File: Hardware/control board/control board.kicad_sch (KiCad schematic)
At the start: 11 parts, among them J1 Screw_Terminal_01x02, SW1 SW_Push

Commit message: updated Board design to v2
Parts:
- added D7: LED, LED_THT:LED_D3.0mm_Clear, symbol Device:LED
- added E10, E9: Conn_01x03_Pin, Connector_PinHeader_2.54mm:PinHeader_1x03_P2.54mm_Vertical, symbol Connector:Conn_01x03_Pin
- added R10: 100, Resistor_SMD:R_0805_2012Metric, symbol Device:R_US
- A1: footprint PCM_arduino-library:Arduino_Mega2560_R3_Shield -> PCM_arduino-library:Arduino_Due_Shield; symbol PCM_arduino-library:Arduino_Mega2560_R3_Shield -> PCM_arduino-library:Arduino_Due_Shield
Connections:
- net GND: now also D7.1 (K), E10.1 (Pin_1), E9.1 (Pin_1)
- net at A1.3V3 (3.3V): now also R10.2
- net at A1.D29: now also E10.3 (Pin_3)
- net at A1.D31: now also E9.3 (Pin_3)
- net at A1.D33: now also E8.3 (Pin_3)
- net at A1.D35: now also E7.3 (Pin_3)
- net at A1.D37: now also E6.3 (Pin_3)
- net at A1.D39: now also E5.3 (Pin_3)
- net at A1.D41: now also E4.3 (Pin_3)
- net at A1.D43: now also E3.3 (Pin_3)
- net at A1.D45: now also E2.3 (Pin_3)
- net at A1.D47: now also E1.3 (Pin_3)
- net PWMD10: no longer names the net of A1.D10 (D10_CS0)
- net PWMD10: no longer E7.3 (Pin_3)
- net PWMD11: no longer names the net of A1.D11
- net PWMD11: no longer E8.3 (Pin_3)
- net PWMD4: no longer names the net of A1.D4 (D4_CS1)
- net PWMD4: no longer E1.3 (Pin_3)
- net PWMD5: no longer names the net of A1.D5
- net PWMD5: no longer E2.3 (Pin_3)
- net PWMD6: no longer names the net of A1.D6
- net PWMD6: no longer E3.3 (Pin_3)
- net PWMD7: no longer names the net of A1.D7
- net PWMD7: no longer E4.3 (Pin_3)
- net PWMD8: no longer names the net of A1.D8
- net PWMD8: no longer E5.3 (Pin_3)
- net PWMD9: no longer names the net of A1.D9
- net PWMD9: no longer E6.3 (Pin_3)
- new net: D7.2 (A), R10.1
- no-connect marks 81 -> 80
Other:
- moved on the sheet: E1, E2, E3, E4, E5, E6, E7, E8, J1, SW1

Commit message: reviewed erc
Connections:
- net GND: no longer A1.GND2 (GND)
- no-connect marks 80 -> 81
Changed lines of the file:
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@@
   (junction (at 187.96 113.665) (diameter 0) (color 0 0 0 0)
-  )
-  (junction (at 23.495 139.7) (diameter 0) (color 0 0 0 0)
   )
   (junction (at 23.495 142.24) (diameter 0) (color 0 0 0 0)
@@
   (no_connect (at 27.305 60.96))
   (no_connect (at 93.345 147.32))
+  (no_connect (at 27.305 139.7))
   (no_connect (at 27.305 48.26))
   (no_connect (at 27.305 40.64))
@@
     (stroke (width 0) (type default))
   )
-  (wire (pts (xy 23.495 137.16) (xy 23.495 139.7))
-    (stroke (width 0) (type default))
-  )
   (wire (pts (xy 135.89 101.6) (xy 142.24 101.6))
     (stroke (width 0) (type default))
@@
     (stroke (width 0) (type default))
   )
+  (wire (pts (xy 135.89 106.68) (xy 146.05 106.68))
+    (stroke (width 0) (type default))
+  )
   (wire (pts (xy 212.09 97.155) (xy 215.9 97.155))
     (stroke (width 0) (type default))
@@
     (stroke (width 0) (type default))
   )
-  (wire (pts (xy 23.495 139.7) (xy 23.495 142.24))
+  (wire (pts (xy 23.495 137.16) (xy 23.495 142.24))
     (stroke (width 0) (type default))
   )
@@
     (stroke (width 0) (type default))
   )
-  (wire (pts (xy 23.495 139.7) (xy 27.305 139.7))
-    (stroke (width 0) (type default))
-  )
   (wire (pts (xy 162.56 97.155) (xy 101.6 97.155))
     (stroke (width 0) (type default))
@@
     (stroke (width 0) (type default))
   )
-  (wire (pts (xy 135.89 106.68) (xy 146.05 106.68))
-    (stroke (width 0) (type default))
-  )

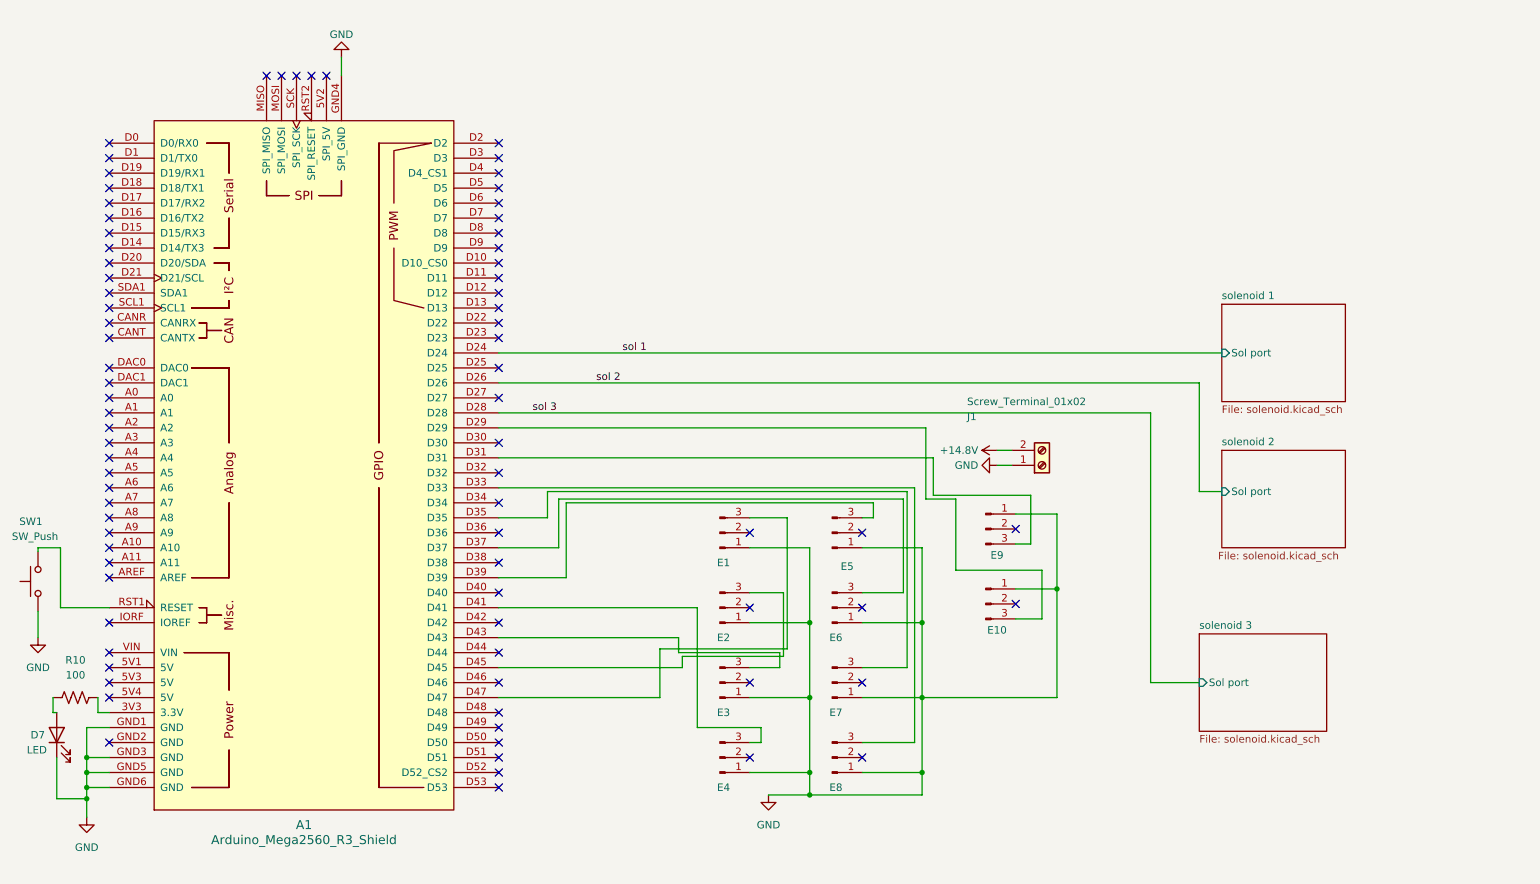
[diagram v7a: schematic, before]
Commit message: cleaned up schematic
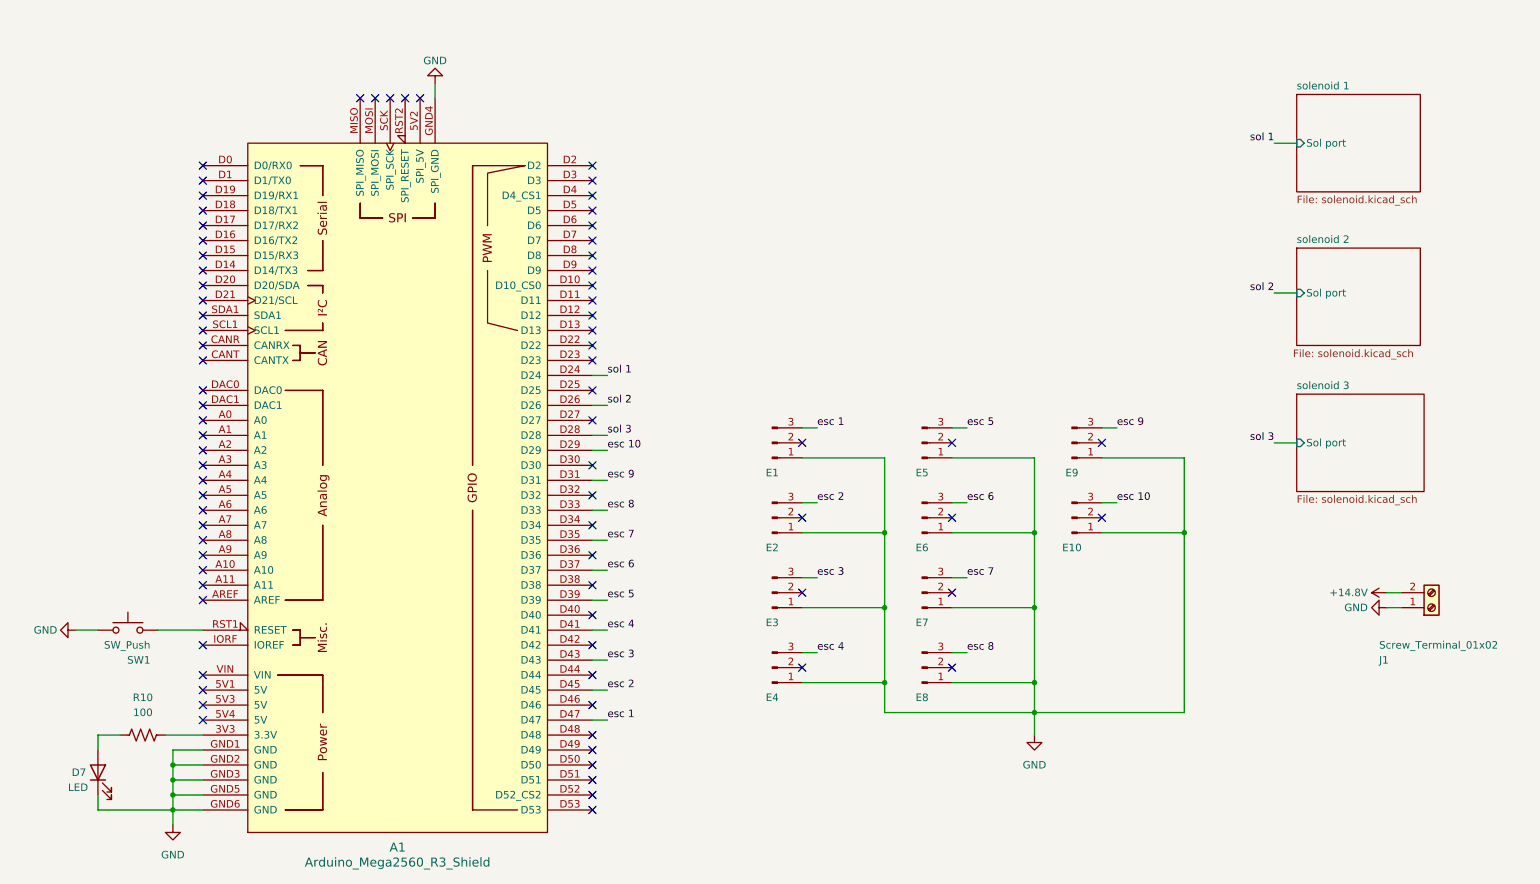
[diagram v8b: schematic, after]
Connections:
- net GND: now also A1.GND2 (GND)
- net esc 10: now reaches A1.D29, E10.3 (Pin_3)
- net esc 9: now reaches A1.D31, E9.3 (Pin_3)
- net esc 8: now reaches A1.D33, E8.3 (Pin_3)
- net esc 7: now reaches A1.D35, E7.3 (Pin_3)
- net esc 6: now reaches A1.D37, E6.3 (Pin_3)
- net esc 5: now reaches A1.D39, E5.3 (Pin_3)
- net esc 4: now reaches A1.D41, E4.3 (Pin_3)
- net esc 3: now reaches A1.D43, E3.3 (Pin_3)
- net esc 2: now reaches A1.D45, E2.3 (Pin_3)
- net esc 1: now reaches A1.D47, E1.3 (Pin_3)
- no-connect marks 81 -> 80
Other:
- moved on the sheet: A1, D7, E1, E10, E2, E3, E4, E5, E6, E7, E8, E9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
